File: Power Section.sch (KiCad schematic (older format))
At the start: 31 parts, among them J1 BATT, J17 Conn_01x03, Q1 IRLML9301TRPBF, Q7 IRLML9301TRPBF, U1 LM1117LDX, U2 LM1117LDX, U3 LM1117LDX, U5 LM1117LDX

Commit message: Resistor numbers and values
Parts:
- gave numbers to parts that had none: 1
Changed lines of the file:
@@
 Connection ~ 5850 4000
 $Comp
-L Device:C_Small C?
+L Device:C_Small C22
 U 1 1 5E6588DD
 P 6900 2600
-F 0 "C?" H 6992 2646 50  0000 L CNN
+F 0 "C22" H 6992 2646 50  0000 L CNN
 F 1 "100uF" H 6992 2555 50  0000 L CNN
 F 2 "Capacitor_SMD:C_0805_2012Metric" H 6900 2600 50  0001 C CNN
@@
 	6900 2500 6950 2500
 $Comp
-L power:GND #PWR?
+L power:GND #PWR0191
 U 1 1 5E658F51
 P 6900 2700
-F 0 "#PWR?" H 6900 2450 50  0001 C CNN
+F 0 "#PWR0191" H 6900 2450 50  0001 C CNN
 F 1 "GND" H 6905 2527 50  0000 C CNN
 F 2 "" H 6900 2700 50  0001 C CNN

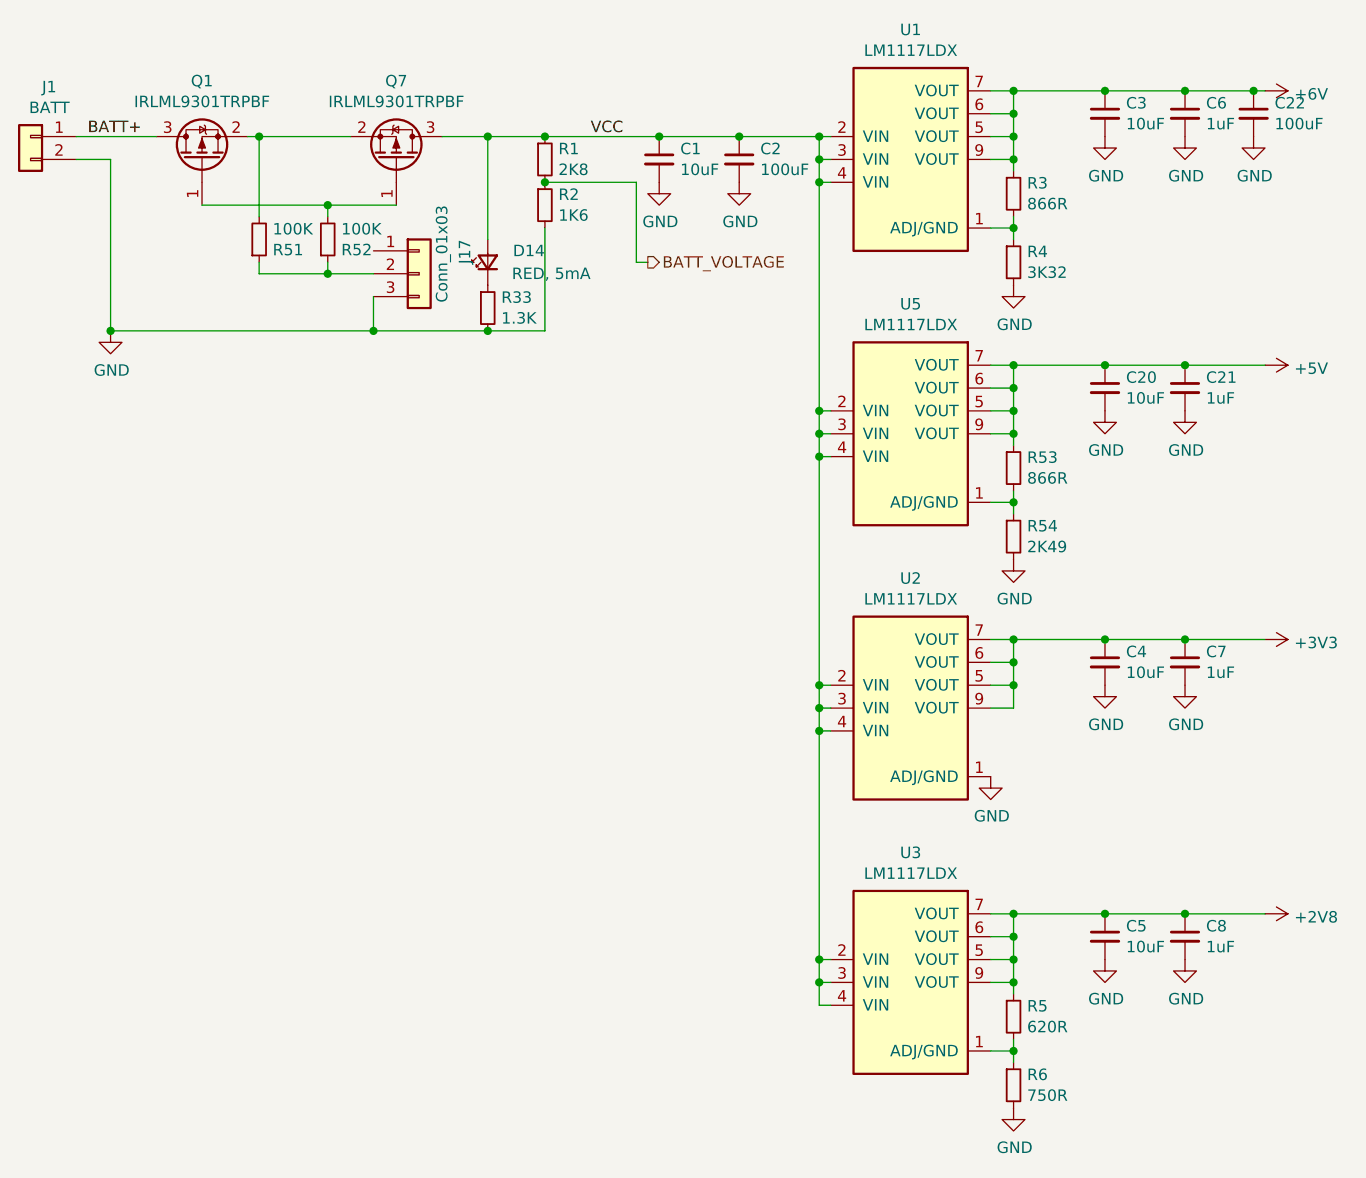
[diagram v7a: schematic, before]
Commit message: Czyszczenie
Usunięto linie 5V oraz 2V8. Poprawiono symbol dla diody RGB
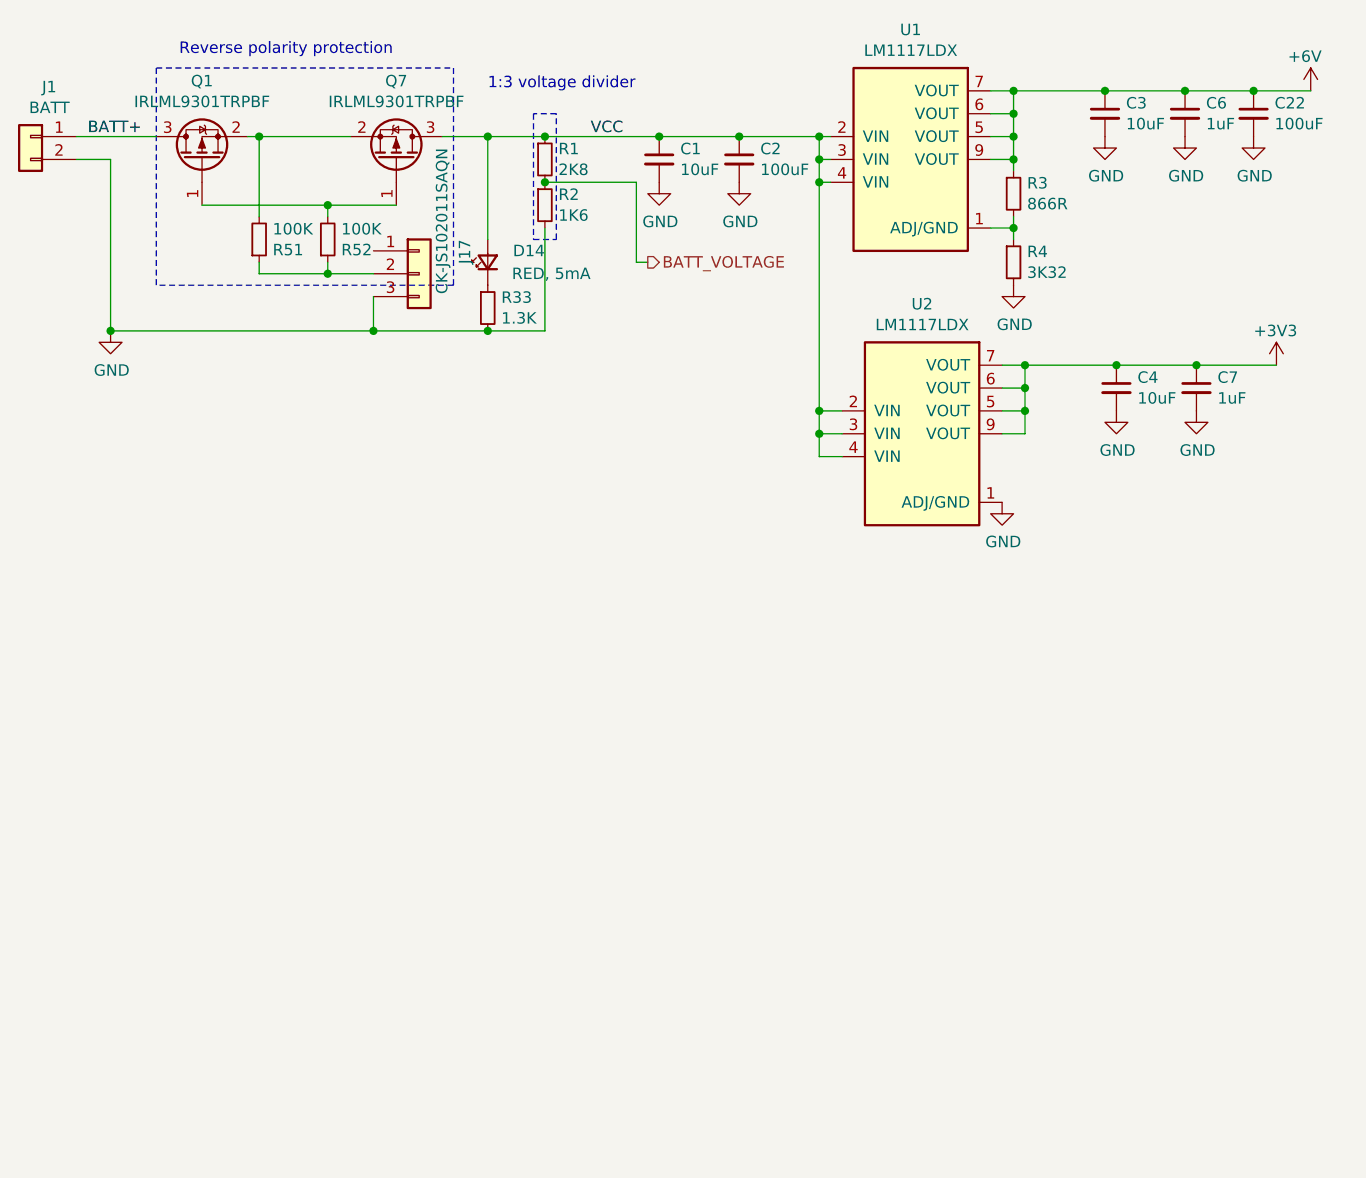
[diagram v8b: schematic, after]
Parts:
- removed C20, C5: 10uF, Capacitor_SMD:C_0603_1608Metric, symbol Device:C_Small
- removed C21, C8: 1uF, Capacitor_SMD:C_0402_1005Metric, symbol Device:C_Small
- removed R5: 620R, Resistor_SMD:R_0402_1005Metric, symbol Device:R_Small
- removed R53: 866R, Resistor_SMD:R_0402_1005Metric, symbol Device:R_Small
- removed R54: 2K49, Resistor_SMD:R_0402_1005Metric, symbol Device:R_Small
- removed R6: 750R, Resistor_SMD:R_0402_1005Metric, symbol Device:R_Small
- removed U3, U5: LM1117LDX, Package_SON:WSON-8_4x4mm_P0.8mm, symbol LM1117:LM1117LDX
- J17: value Conn_01x03 -> CK-JS102011SAQN
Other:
- note added: "1:3 voltage divider"
- note added: "Reverse polarity protection"
- moved on the sheet: C4, C7, U2
